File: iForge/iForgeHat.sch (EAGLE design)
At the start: 5 parts

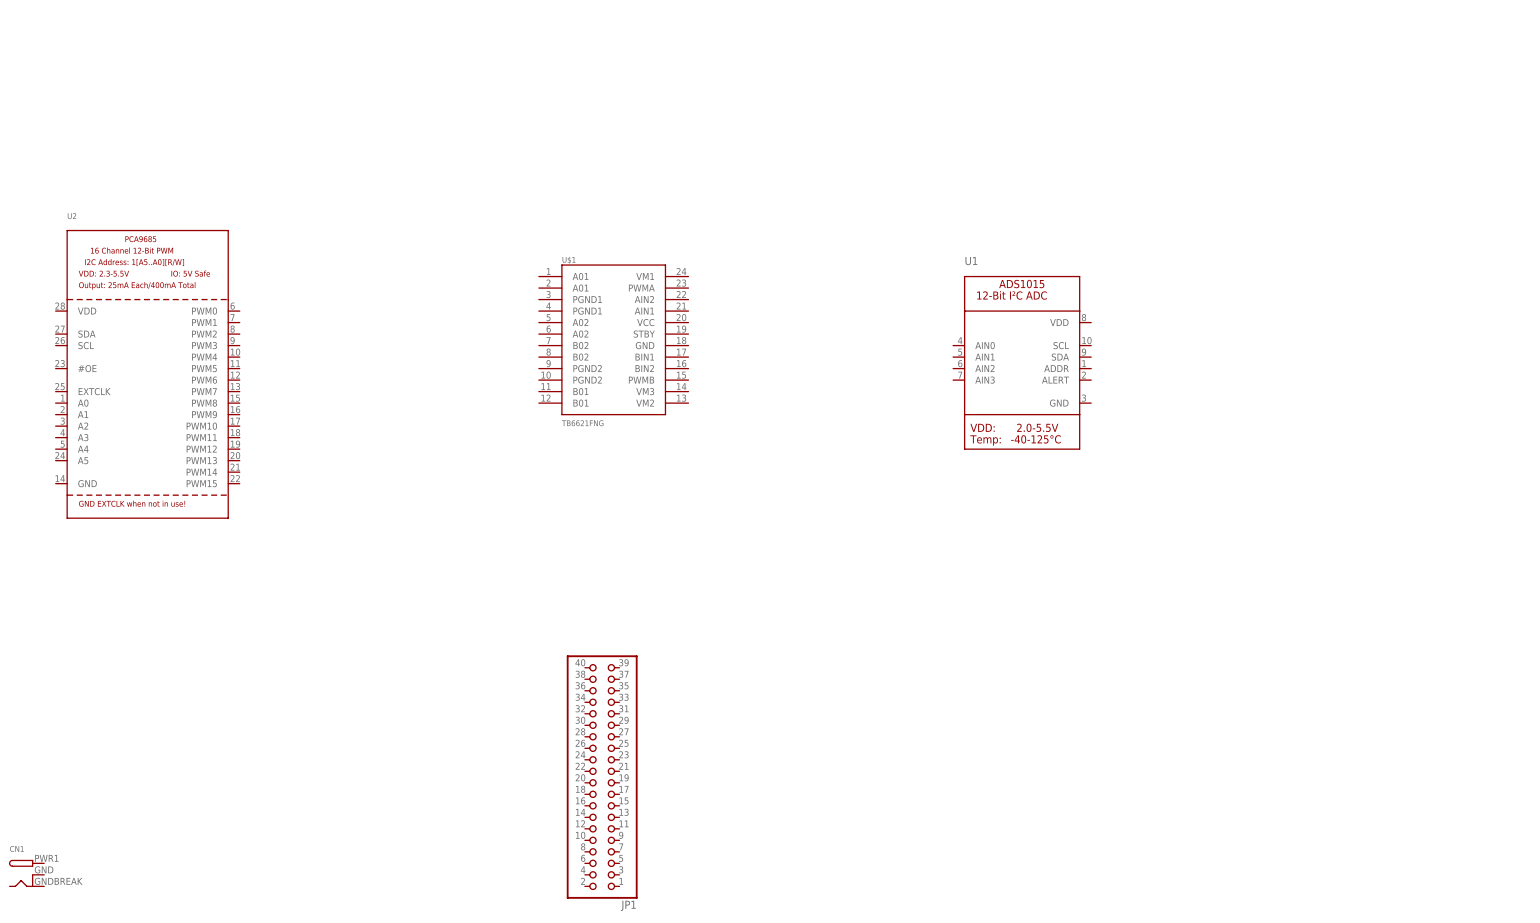
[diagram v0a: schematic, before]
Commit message: added routing for adc and began h-bridge
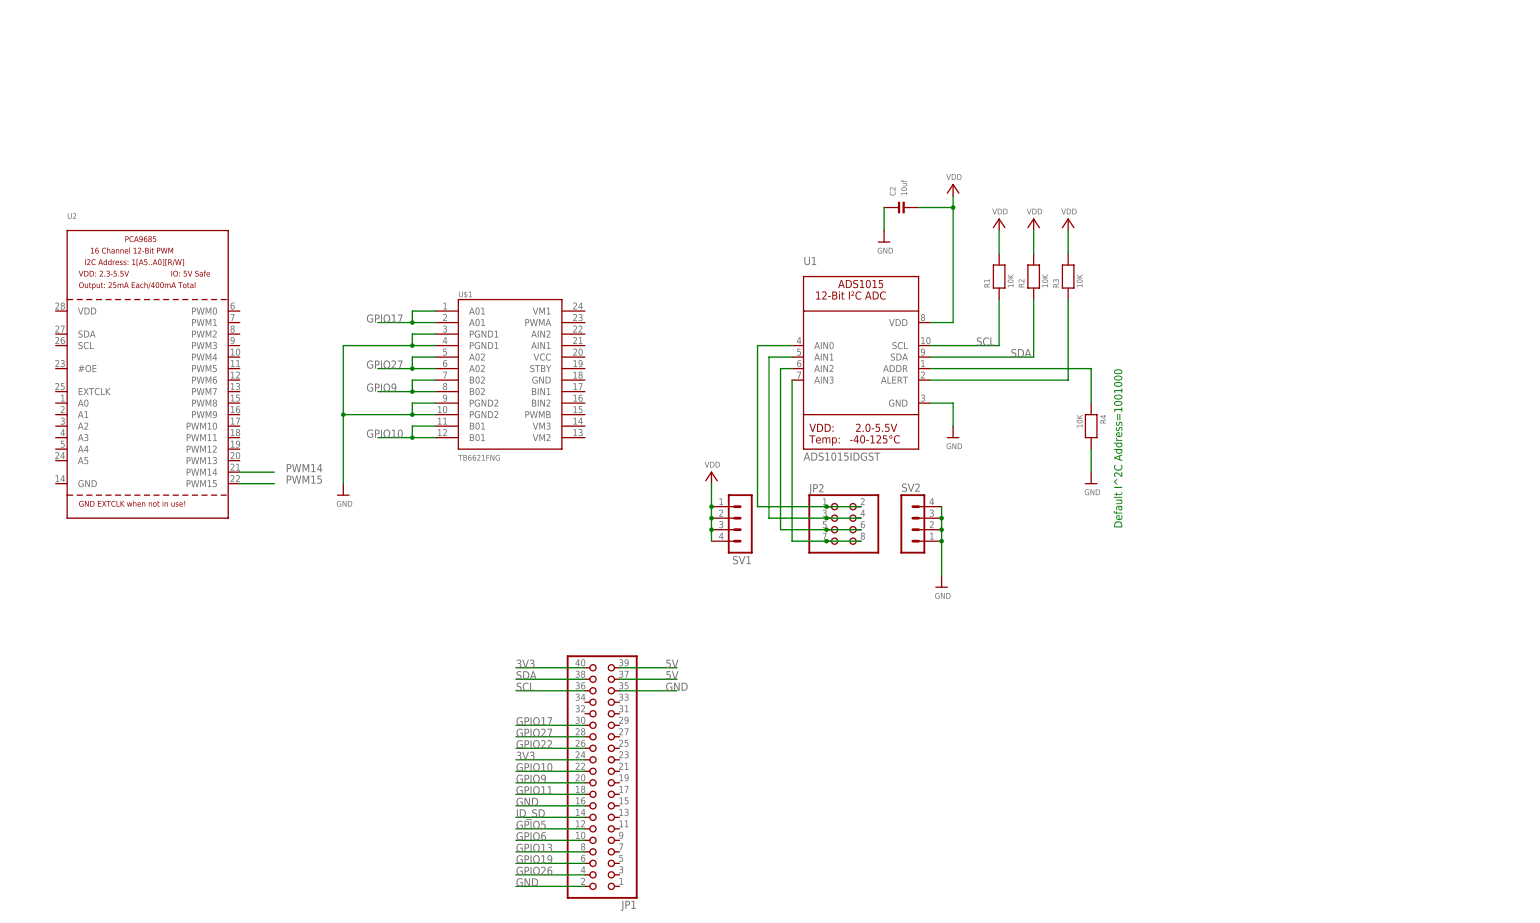
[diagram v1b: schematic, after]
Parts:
- removed CN1: (no value), adafruit:DCBARRELSMT
- added C2: 10uf, adc1015microbuilder:CAP_CERAMIC0402
- added JP2: (no value), adafruit:PINHD-2X4
- added R1, R2, R3, R4: 10K, adc1015microbuilder:RESISTOR0402
- added SV1, SV2: (no value), con-lstb:MA04-1
- U1: value (none) -> ADS1015IDGST
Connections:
- new net 3V3: JP1.24, JP1.40
- new net 5V: JP1.37, JP1.39
- new net GND: C2.P$1, JP1.16, JP1.2, JP1.35, R4.2, SV2.1, SV2.2, SV2.3, SV2.4, U$1.PGND1@3, U$1.PGND1@4, U$1.PGND2@10, U$1.PGND2@9, U1.GND
- new net GPIO10: JP1.22, U$1.B01@11, U$1.B01@12
- new net GPIO11: JP1.18
- new net GPIO13: JP1.8
- new net GPIO17: JP1.30, U$1.A01@1, U$1.A01@2
- new net GPIO19: JP1.6
- new net GPIO22: JP1.26
- new net GPIO26: JP1.4
- new net GPIO27: JP1.28, U$1.A02@5, U$1.A02@6
- new net GPIO5: JP1.12
- new net GPIO6: JP1.10
- new net GPIO9: JP1.20, U$1.B02@7, U$1.B02@8
- new net ID_SD: JP1.14
- new net N$10: JP2.7, JP2.8, U1.AIN3
- new net N$3: R3.1, U1.ALERT
- new net N$4: R4.1, U1.ADDR
- new net N$7: JP2.1, JP2.2, U1.AIN0
- new net N$8: JP2.3, JP2.4, U1.AIN1
- new net N$9: JP2.5, JP2.6, U1.AIN2
- new net PWM14: U2.PWM14
- new net PWM15: U2.PWM15
- new net SCL: JP1.36, R1.1, U1.SCL
- new net SDA: JP1.38, R2.1, U1.SDA
- new net VDD: C2.P$2, R1.2, R2.2, R3.2, SV1.1, SV1.2, SV1.3, SV1.4, U1.VDD
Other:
- note added: "Default I^2C Address=1001000"
- moved on the sheet: U$1, U1

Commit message: finished schematic todo: solve power
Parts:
- removed U$1: TB6621FNG, SparkFun:TB6621FNG
- added C1: 10uF, adc1015microbuilder:CAP_CERAMIC0402
- added C3: 0.1uF, adc1015microbuilder:CAP_CERAMIC0402
- added C4: 0.1 uF, adc1015microbuilder:CAP_CERAMIC0402
- added C5: (no value), adc1015microbuilder:CAP_CERAMIC0402
- added J1, J10, J11, J12, J13, J14, J2, J3, J4, J5, J6, J7, J8, J9: (no value), SparkFun-Connectors:CONN_03
- added J15, J16: (no value), SparkFun-Connectors:CONN_02SPRING-2.54-RA
- added J17: CONN_12X2, SparkFun-Connectors:CONN_12X2
- added J18: 5.5x2.1mm Barrel, SparkFun-Connectors:POWER_JACKSMD
- added R10, R12, R13, R14, R15, R16, R17, R18, R19, R5, R6, R7, R8, R9: 220, adc1015microbuilder:RESISTOR0402
- added R11: 10k, adc1015microbuilder:RESISTOR0402
- added U3: TB6621FNG, SparkFun:TB6621FNG
- C2: value 10uf -> 10uF; device adc1015microbuilder:CAP_CERAMIC0402 -> adafruit:SUPERCAP
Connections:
- new net A01: J15.2, U3.A01@1, U3.A01@2
- new net A02: J15.1, U3.A02@5, U3.A02@6
- new net B01: J16.2, U3.B01@11, U3.B01@12
- new net B02: J16.1, U3.B02@7, U3.B02@8
- new net GPIO12: J17.13, JP1.9
- new net GPIO14: J17.15, JP1.33
- new net GPIO15: J17.16, JP1.31
- new net GPIO16: J17.17, JP1.5
- new net GPIO18: J17.19, JP1.29
- new net GPIO20: J17.21, JP1.3
- new net GPIO21: J17.22, JP1.1
- new net GPIO23: J17.24, JP1.25
- new net GPIO24: JP1.23, U3.AIN1
- new net GPIO25: JP1.19, U3.AIN2
- new net GPIO4: J17.5, JP1.34
- new net GPIO7: J17.8, JP1.15
- new net GPIO8: J17.9, JP1.17
- new net ID_SC: JP1.13
- new net N$1: R11.1, U2.#OE
- new net N$11: J6.1, R10.2
- new net N$12: J7.1, R12.2
- new net N$13: J9.1, R14.2
- new net N$14: J5.1, R9.2
- new net N$15: J4.1, R8.2
- new net N$16: J3.1, R7.2
- new net N$17: J2.1, R6.2
- new net N$18: J1.1, R5.2
- new net N$19: J13.1, R18.2
- new net N$2: J14.1, R19.2
- new net N$20: J8.1, R13.2
- new net N$21: J10.1, R15.2
- new net N$5: J11.1, R16.2
- new net N$6: J12.1, R17.2
- new net PWM0: R5.1, U2.PWM0
- new net PWM1: R6.1, U2.PWM1
- new net PWM10: R16.1, U2.PWM10
- new net PWM11: R17.1, U2.PWM11
- new net PWM12: R18.1, U2.PWM12
- new net PWM13: R19.1, U2.PWM13
- new net PWM2: R7.1, U2.PWM2
- new net PWM3: R8.1, U2.PWM3
- new net PWM4: R9.1, U2.PWM4
- new net PWM5: R10.1, U2.PWM5
- new net PWM6: R12.1, U2.PWM6
- new net PWM7: R13.1, U2.PWM7
- new net PWM8: R14.1, U2.PWM8
- new net PWM9: R15.1, U2.PWM9
- new net VM: C2.+, C3.P$1, U3.VM1, U3.VM2, U3.VM3
- net 3V3: now also J17.2
- net 5V: now also J17.1
- net GND: now also C1.P$1, C2.-, C3.P$2, C4.P$1, C5.P$1, J1.3, J10.3, J11.3, J12.3, J13.3, J14.3, J17.3, J17.4, J2.3, J3.3, J4.3, J5.3, J6.3, J7.3, J8.3, J9.3, JP1.11, JP1.21, JP1.27, JP1.32, JP1.7, R11.2, U2.A0, U2.A1, U2.A2, U2.A3, U2.A4, U2.A5, U2.EXTCLK, U2.GND, U3.GND, U3.PGND1@3, U3.PGND1@4, U3.PGND2@10, U3.PGND2@9; no longer C2.P$1, U$1.PGND1@3, U$1.PGND1@4, U$1.PGND2@10, U$1.PGND2@9
- net GPIO10: now also J17.11; no longer U$1.B01@11, U$1.B01@12
- net GPIO11: now also J17.12
- net GPIO13: now also J17.14
- net GPIO17: now also J17.18; no longer U$1.A01@1, U$1.A01@2
- net GPIO19: now also J17.20
- net GPIO22: now also J17.23
- net GPIO26: now also U3.BIN1
- net GPIO27: now also U3.BIN2; no longer U$1.A02@5, U$1.A02@6
- net GPIO5: now also J17.6
- net GPIO6: now also J17.7
- net GPIO9: now also J17.10; no longer U$1.B02@7, U$1.B02@8
- net PWM14: now also U3.PWMA
- net PWM15: now also U3.PWMB
- net SCL: now also U2.SCL
- net SDA: now also U2.SDA
- net VDD: now also C1.P$2, C4.P$2, C5.P$2, J1.2, J10.2, J11.2, J12.2, J13.2, J14.2, J2.2, J3.2, J4.2, J5.2, J6.2, J7.2, J8.2, J9.2, U2.VDD, U3.STBY, U3.VCC; no longer C2.P$2
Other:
- note added: "Genesis Learning"
